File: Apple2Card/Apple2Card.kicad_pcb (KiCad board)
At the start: 2 copper layers, 160 x 78.2 mm, 57 parts, among them J1 ICSP, J2 Conn_01x25, J3 Conn_01x25, J4 Conn_01x10, J5 Conn_01x04, SW1 SW_Push, U1 ATmega328P-P, U2 74HC32, U3 74HC00, U4 74HC373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

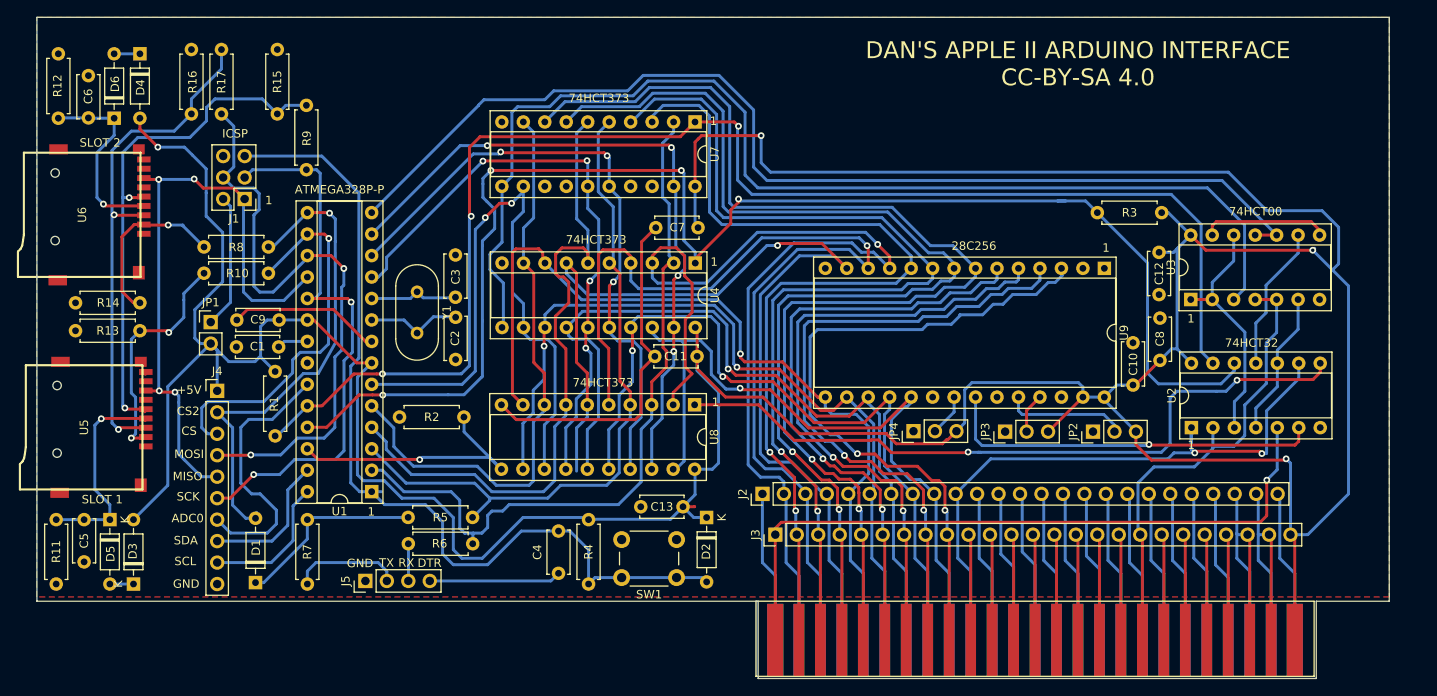
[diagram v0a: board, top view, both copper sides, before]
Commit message: Swapped OR with AND
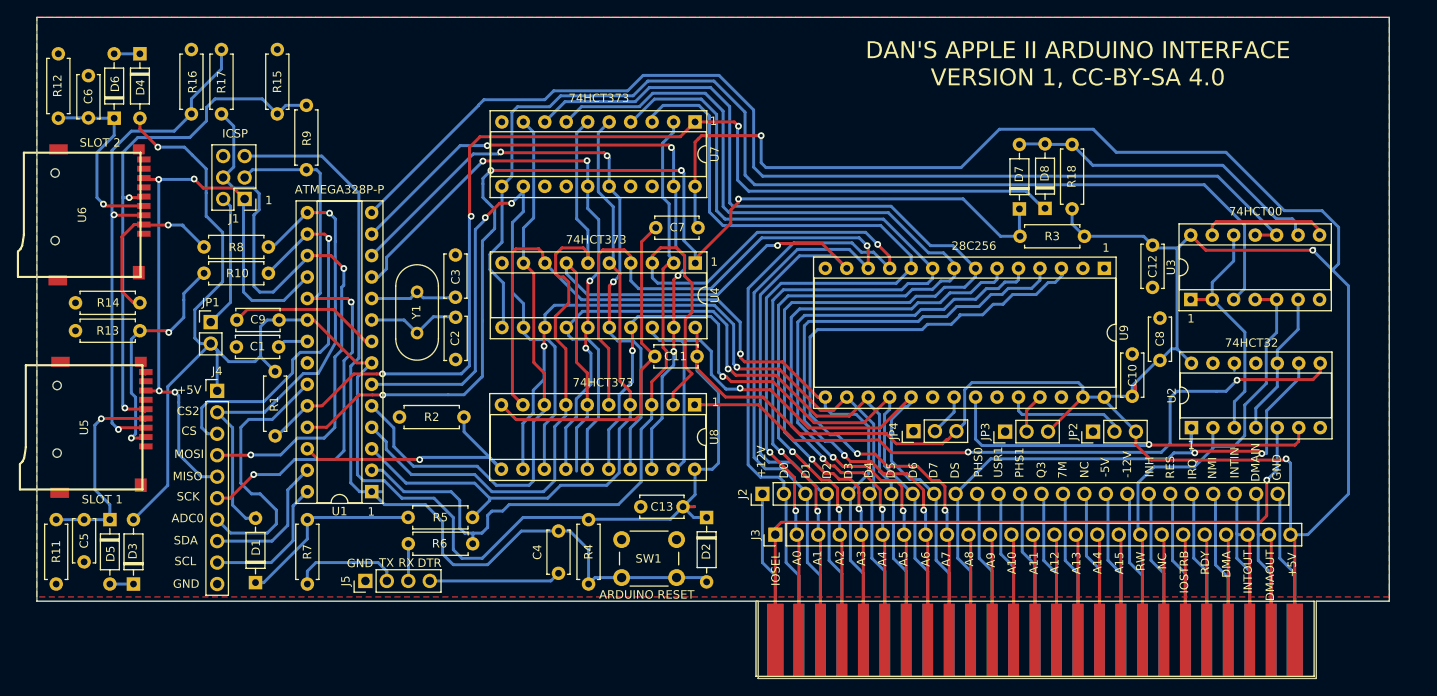
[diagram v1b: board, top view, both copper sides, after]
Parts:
- added D7: 1N4148, Diode_THT:D_DO-35_SOD27_P7.62mm_Horizontal, F.Cu at (149.3, 48.1)
- added D8: 1N4148, Diode_THT:D_DO-35_SOD27_P7.62mm_Horizontal, F.Cu at (152.3, 48.0)
- added R18: 10k, Resistor_THT:R_Axial_DIN0207_L6.3mm_D2.5mm_P7.62mm_Horizontal, F.Cu at (155.5, 48.1)
- moved R3 9.56 mm to (149.4, 51.3)
- moved C10 1.33 mm to (162.6, 70.2)
- moved C12 1.15 mm to (165.0, 52.4)
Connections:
- U2 pad 11: Net-(U2-Pad11) -> unconnected-(U2-Pad11)
- U2 pad 12: INEN -> GND
- U2 pad 13: INADR -> GND
- U3 pad 9: Net-(U2-Pad11) -> Net-(U3-Pad9)
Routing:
- net INEN: track 172.0 -> 131.5 mm
- net Net-(U3-Pad9): track 0.00 -> 38.2 mm
- net INADR: track 166.2 -> 129.9 mm
- net Net-(U2-Pad11): track 17.2 -> 0.00 mm
- net +5V: track 491.8 -> 507.5 mm
- net GND: track 78.5 -> 80.0 mm
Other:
- board text added: "+12V"
- board text added: "-12V"
- board text added: "-5V"
- board text added: "7M"
- board text added: "A0"
- board text added: "A1"
- board text added: "A10"
- board text added: "A11"
- board text added: "A12"
- board text added: "A13"
- board text added: "A14"
- board text added: "A15"
- board text added: "A2"
- board text added: "A3"
- board text added: "A4"
- board text added: "A5"
- board text added: "A6"
- board text added: "A7"
- board text added: "A8"
- board text added: "A9"
- board text added: "ARDUINO RESET"
- board text added: "D0"
- board text added: "D1"
- board text added: "D2"
- board text added: "D3"
- board text added: "D4"
- board text added: "D5"
- board text added: "D6"
- board text added: "D7"
- board text added: "DAN'S APPLE II ARDUINO INTERFACE VERSION 1, CC-BY-SA 4.0"
- board text added: "DMA"
- board text added: "DMAIN"
- board text added: "DMAOUT"
- board text added: "DS"
- board text added: "INH"
- board text added: "INTIN"
- board text added: "INTOUT"
- board text added: "IOSEL"
- board text added: "IOSTRB"
- board text added: "IRQ"
- board text added: "NC"
- board text added: "NMI"
- board text added: "PHS0"
- board text added: "PHS1"
- board text added: "Q3"
- board text added: "RDY"
- board text added: "RES"
- board text added: "RW"
- board text added: "USR1"
- board text removed: "DAN'S APPLE II ARDUINO INTERFACE CC-BY-SA 4.0"

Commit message: Add power supply bypass jumpers for power supply variations
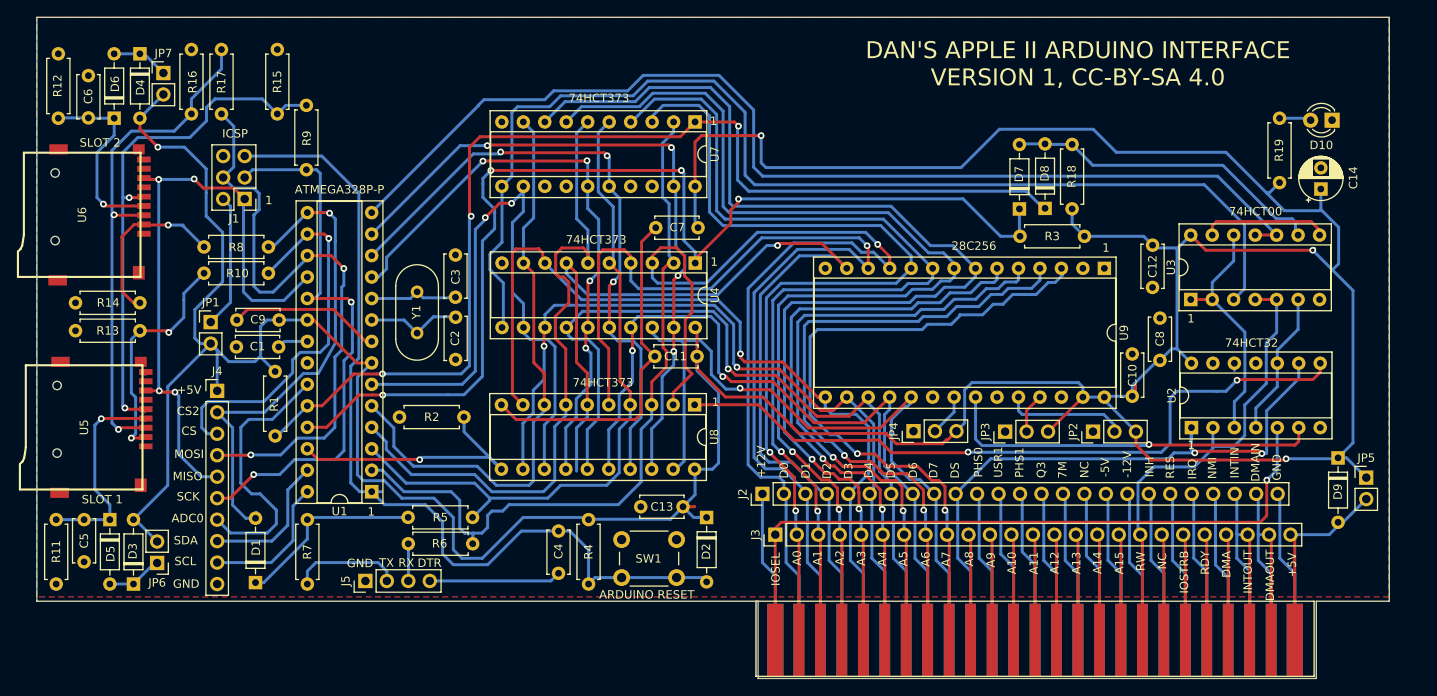
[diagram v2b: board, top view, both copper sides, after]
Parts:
- added C14: 10 uF, Capacitor_THT:CP_Radial_D5.0mm_P2.50mm, F.Cu at (184.9, 45.7)
- added D10: LED, LED_THT:LED_D3.0mm, F.Cu at (186.3, 37.6)
- added D9: 1N4148, Diode_THT:D_DO-35_SOD27_P7.62mm_Horizontal, F.Cu at (187.0, 77.5)
- added JP5: VDROP, Connector_PinHeader_2.54mm:PinHeader_1x02_P2.54mm_Vertical, F.Cu at (190.3, 79.9)
- added JP6: VDROP, Connector_PinHeader_2.54mm:PinHeader_1x02_P2.54mm_Vertical, F.Cu at (47.2, 90.0)
- added JP7: VDROP, Connector_PinHeader_2.54mm:PinHeader_1x02_P2.54mm_Vertical, F.Cu at (48.0, 32.0)
- added R19: 1k, Resistor_THT:R_Axial_DIN0207_L6.3mm_D2.5mm_P7.62mm_Horizontal, F.Cu at (180.1, 45.0)
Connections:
- BUS1 pad 25: +5V -> Net-(BUS1-Pad25)
- J3 pad 25: +5V -> Net-(BUS1-Pad25)
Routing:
- net Net-(BUS1-Pad25): track 0.00 -> 26.5 mm
- net +5V: track 507.5 -> 493.5 mm
- net Net-(D3-Pad1): track 2.79 -> 6.63 mm
- net Net-(D10-Pad2): track 0.00 -> 3.77 mm
- net Net-(D4-Pad1): track 3.05 -> 6.77 mm

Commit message: try committing again
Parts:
- moved D4 0.62 mm to (44.6, 29.6)
- moved D3 0.43 mm to (44.0, 92.5)
- moved D6 0.33 mm to (41.9, 37.2)
- moved D5 0.24 mm to (41.4, 84.8)
- moved C6 0.23 mm to (38.9, 37.3)
- moved C5 0.13 mm to (38.5, 84.8)
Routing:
- net D2: track 124.7 -> 116.4 mm
- net +5V: track 493.5 -> 489.7 mm
- net Net-(BUS1-Pad25): track 26.5 -> 23.6 mm
- net GND: track 80.0 -> 78.5 mm
- net RESET: track 106.7 -> 105.5 mm
- net DS: track 73.3 -> 72.2 mm
- net CS2: track 58.4 -> 57.7 mm
- net D0: track 125.8 -> 125.2 mm

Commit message: Before changing to 8255
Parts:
- moved JP2 10.5 mm to (147.5, 74.1)
- moved JP3 10.3 mm to (157.8, 74.2)
- moved D9 3.34 mm to (186.2, 80.8)
- moved JP5 2.67 mm to (189.3, 82.3)
- moved JP4 0.20 mm to (136.8, 74.2)
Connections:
- BUS1 pad 25: Net-(BUS1-Pad25) -> +5V
- D9 pad 2: Net-(BUS1-Pad25) -> +5V
- J3 pad 25: Net-(BUS1-Pad25) -> +5V
- JP5 pad 2: Net-(BUS1-Pad25) -> +5V
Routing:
- net +5V: track 489.7 -> 581.0 mm, vias 4 -> 5
- net Net-(BUS1-Pad25): track 23.6 -> 0.00 mm
- net Net-(JP2-Pad2): track 14.4 -> 4.15 mm
- net Net-(JP3-Pad2): track 4.74 -> 11.5 mm
- net IOSEL: track 82.9 -> 81.5 mm
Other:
- board text added: "DAN'S APPLE II SD CARD ARDUINO INTERFACE VERSION 1, CC-BY-SA 4.0"
- board text added: "DROP VOLTAGE"
- board text removed: "DAN'S APPLE II ARDUINO INTERFACE VERSION 1, CC-BY-SA 4.0"

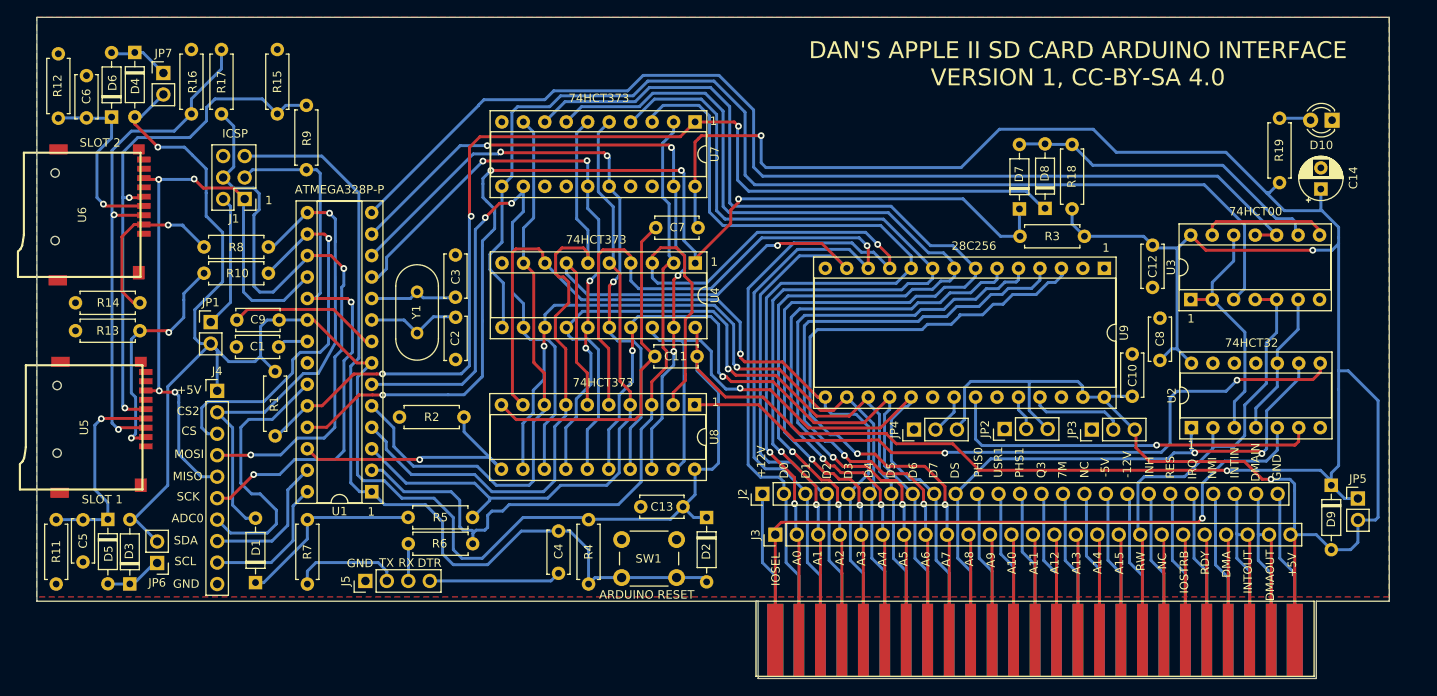
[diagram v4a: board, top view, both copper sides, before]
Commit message: Changed to 8255
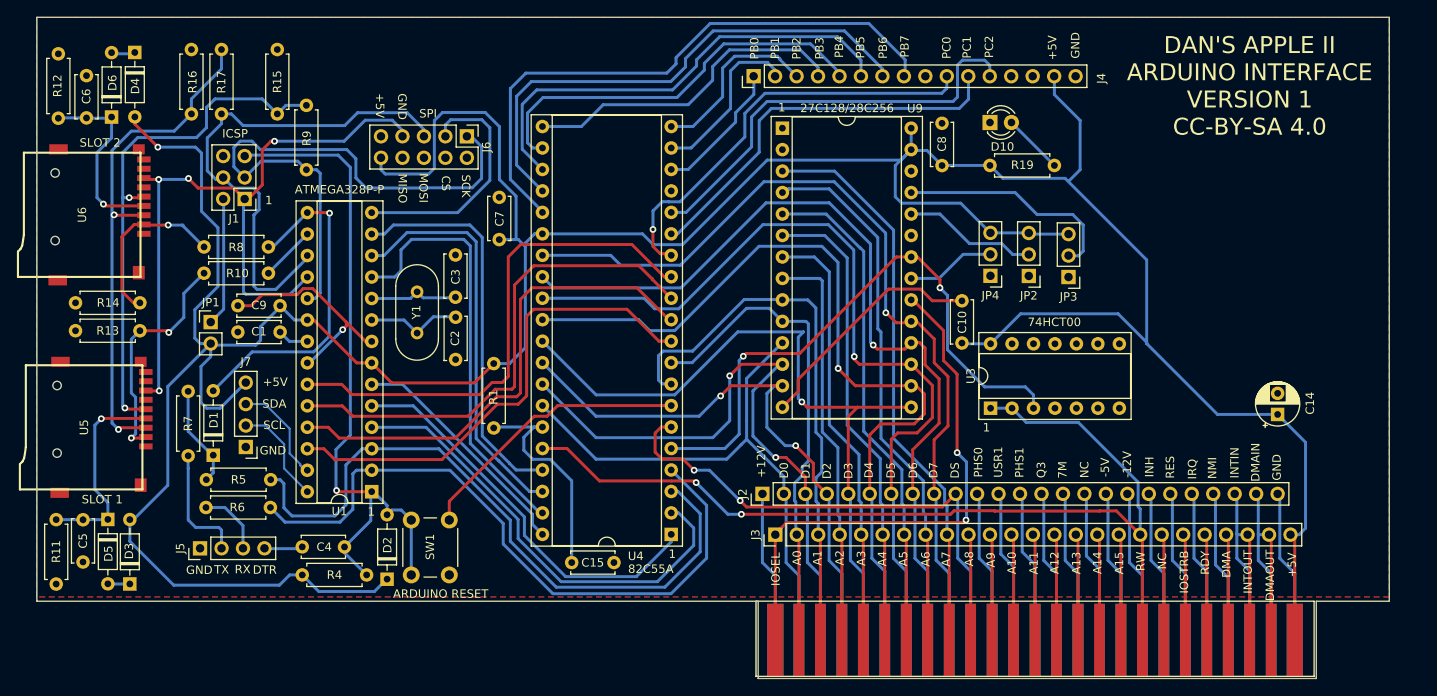
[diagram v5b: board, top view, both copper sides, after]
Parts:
- removed C11, C12, C13: 100 nF, Capacitor_THT:C_Disc_D5.0mm_W2.5mm_P5.00mm
- removed D7, D8, D9: 1N4148, Diode_THT:D_DO-35_SOD27_P7.62mm_Horizontal
- removed JP5, JP6, JP7: VDROP, Connector_PinHeader_2.54mm:PinHeader_1x02_P2.54mm_Vertical
- removed R18, R2, R3: 10k, Resistor_THT:R_Axial_DIN0207_L6.3mm_D2.5mm_P7.62mm_Horizontal
- removed U2: 74HC32, Package_DIP:DIP-14_W7.62mm_Socket
- removed U7, U8: 74HC373, Package_DIP:DIP-20_W7.62mm_Socket
- added C15: 100 nF, Capacitor_THT:C_Disc_D5.0mm_W2.5mm_P5.00mm, F.Cu at (96.3, 89.9)
- added J6: WIZNET 5500, Connector_PinHeader_2.54mm:PinHeader_2x05_P2.54mm_Vertical, F.Cu at (83.9, 39.5)
- added J7: Conn_01x04, Connector_PinHeader_2.54mm:PinHeader_1x04_P2.54mm_Vertical, F.Cu at (57.7, 76.2)
- J4: value Conn_01x10 -> Conn_01x16; footprint Connector_PinHeader_2.54mm:PinHeader_1x10_P2.54mm_Vertical -> Connector_PinHeader_2.54mm:PinHeader_1x16_P2.54mm_Vertical
- R1: value 10k -> 1k
- U3: value 74HC00 -> 74HCT00
- U4: value 74HC373 -> 82C55A; footprint Package_DIP:DIP-20_W7.62mm_Socket -> Package_DIP:DIP-40_W15.24mm_Socket
- moved J4 73.6 mm to (117.8, 32.4), turned to 90 degrees
- moved U9 41.5 mm to (121.2, 38.5), turned to 0 degrees
- moved D10 40.5 mm to (145.8, 37.8), turned to 0 degrees
- moved D2 38.5 mm to (74.5, 91.9), turned to 90 degrees
- moved C8 34.6 mm to (140.1, 42.9)
- moved R4 34.5 mm to (64.4, 91.4), turned to 0 degrees
- moved R19 34.3 mm to (145.8, 42.9), turned to 0 degrees
- moved U4 32.2 mm to (108.1, 86.6), turned to 180 degrees
- moved SW1 31.4 mm to (77.3, 91.4), turned to 90 degrees
- moved C4 30.5 mm to (64.4, 88.1), turned to 0 degrees
- moved C14 27.2 mm to (179.8, 72.4)
- moved U3 27.0 mm to (145.9, 71.7)
- moved R1 25.9 mm to (87.1, 74.0)
- moved R6 24.3 mm to (53.0, 83.4)
- moved R5 24.3 mm to (53.1, 80.1)
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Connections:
- J4 pad 1: +5V -> Net-(J4-Pad1)
- J4 pad 10: GND -> Net-(J4-Pad10)
- J4 pad 2: CS2 -> Net-(J4-Pad2)
- J4 pad 3: CS -> Net-(J4-Pad3)
- J4 pad 4: MOSI -> Net-(J4-Pad4)
- J4 pad 5: MISO -> Net-(J4-Pad5)
- J4 pad 6: SCK -> Net-(J4-Pad6)
- J4 pad 7: PC0 -> Net-(J4-Pad7)
- J4 pad 8: PC4 -> Net-(J4-Pad8)
- J4 pad 9: PC5 -> unconnected-(J4-Pad9)
- R1 pad 1: INADR -> Net-(C15-Pad1)
- U1 pad 14: SETV -> CS3
- U1 pad 23: PC0 -> OBFA
- U1 pad 24: INADR -> ACKA
- U1 pad 25: INEN -> STBA
- U1 pad 26: OUTEN -> IBFA
- U3 pad 1: Net-(U2-Pad3) -> RW
- U3 pad 10: SETV -> GND
- U3 pad 11: SETV -> unconnected-(U3-Pad11)
- U3 pad 12: Net-(U2-Pad3) -> GND
- U3 pad 13: Net-(U3-Pad13) -> GND
- U3 pad 2: Net-(U2-Pad3) -> RW
- U3 pad 4: RW -> GND
- U3 pad 5: RW -> GND
- U3 pad 6: Net-(U2-Pad10) -> unconnected-(U3-Pad6)
- U3 pad 8: Net-(U3-Pad13) -> unconnected-(U3-Pad8)
- U3 pad 9: Net-(D7-Pad2) -> GND
- U4 pad 1: INEN -> PD3
- U4 pad 10: GND -> IBFA
- U4 pad 11: Net-(U3-Pad3) -> STBA
- U4 pad 12: PD4 -> ACKA
- U4 pad 13: D4 -> OBFA
- U4 pad 14: D5 -> Net-(J4-Pad10)
- U4 pad 15: PD5 -> Net-(J4-Pad11)
- U4 pad 16: PD6 -> Net-(J4-Pad12)
- U4 pad 17: D6 -> unconnected-(U4-Pad17)
- U4 pad 18: D7 -> Net-(J4-Pad1)
- U4 pad 19: PD7 -> Net-(J4-Pad2)
- U4 pad 2: PD0 -> PD2
- U4 pad 20: +5V -> Net-(J4-Pad3)
- U4 pad 3: D0 -> PD1
- U4 pad 4: D1 -> PD0
- U4 pad 5: PD1 -> Net-(U3-Pad3)
- U4 pad 6: PD2 -> DS
- U4 pad 7: D2 -> GND
- U4 pad 8: D3 -> A1
- U4 pad 9: PD3 -> A0
- U9 pad 20: GND -> IOSEL
- U9 pad 22: Net-(U2-Pad6) -> Net-(U3-Pad3)
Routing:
- net +5V: track 581.0 -> 423.9 mm, vias 5 -> 1
- net INEN: track 131.5 -> 0.00 mm, vias 4 -> 0
- net INADR: track 129.9 -> 0.00 mm, vias 3 -> 0
- net SETV: track 128.2 -> 0.00 mm
- net A3: track 137.7 -> 51.5 mm, vias 2 -> 0
- net Net-(U2-Pad8): track 84.6 -> 0.00 mm, vias 2 -> 0
- net A2: track 129.3 -> 48.3 mm, vias 2 -> 0
- net Net-(J4-Pad8): track 0.00 -> 70.3 mm
- net Net-(U3-Pad3): track 136.3 -> 70.0 mm, vias 0 -> 2
- net Net-(J4-Pad7): track 0.00 -> 62.3 mm
- net OBFA: track 0.00 -> 60.8 mm
- net ACKA: track 0.00 -> 59.6 mm
- net STBA: track 0.00 -> 59.0 mm
- net RW: track 56.3 -> 115.3 mm, vias 0 -> 2
- net IBFA: track 0.00 -> 58.0 mm
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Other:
- board text added: "27C128/28C256"
- board text added: "82C55A"
- board text added: "DAN'S APPLE II ARDUINO INTERFACE VERSION 1 CC-BY-SA 4.0"
- board text added: "PB0"
- board text added: "PB1"
- board text added: "PB2"
- board text added: "PB3"
- board text added: "PB4"
- board text added: "PB5"
- board text added: "PB6"
- board text added: "PB7"
- board text added: "PC0"
- board text added: "PC1"
- board text added: "PC2"
- board text added: "SPI"
- board text removed: "28C256"
- board text removed: "74HCT32"
- board text removed: "74HCT373"
- board text removed: "ADC0"
- board text removed: "CS2"
- board text removed: "DAN'S APPLE II SD CARD ARDUINO INTERFACE VERSION 1, CC-BY-SA 4.0"
- board text removed: "DROP VOLTAGE"
